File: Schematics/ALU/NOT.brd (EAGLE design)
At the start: 53.6 x 60 mm, 24 parts

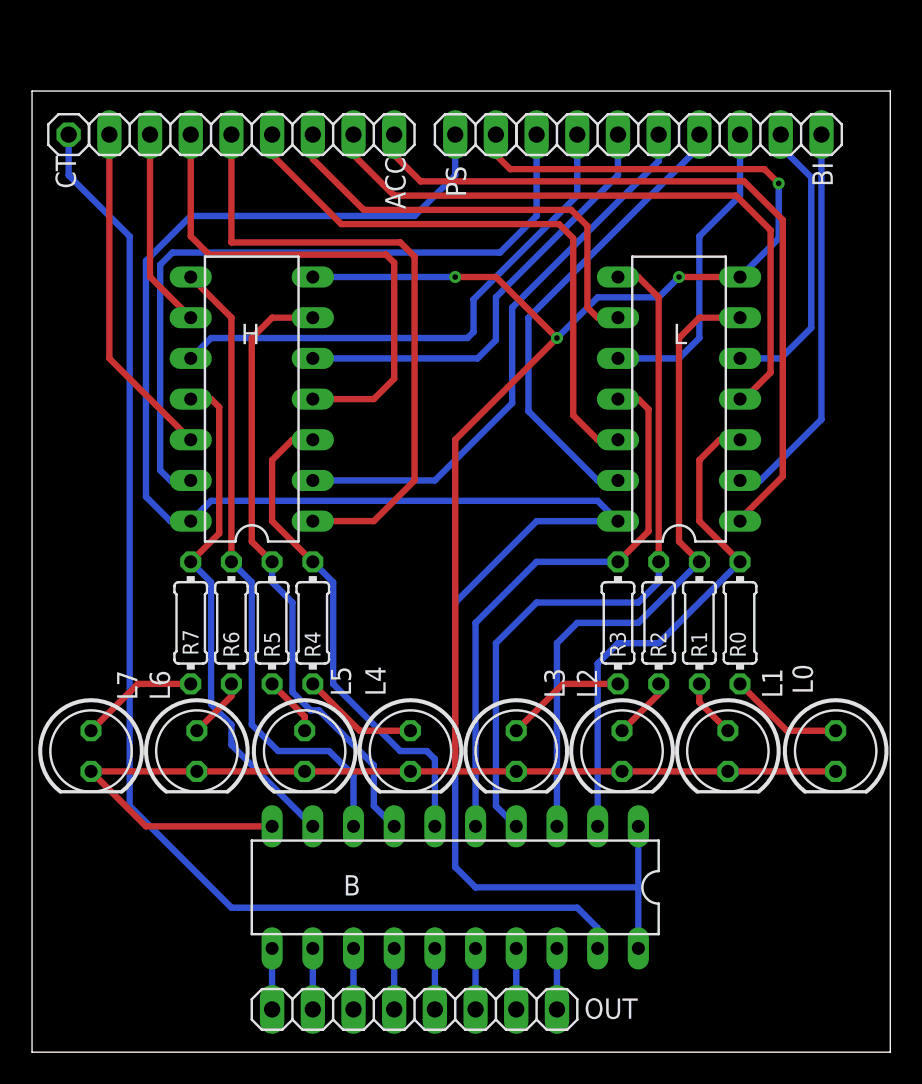
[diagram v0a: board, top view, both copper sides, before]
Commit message: Added NOT.
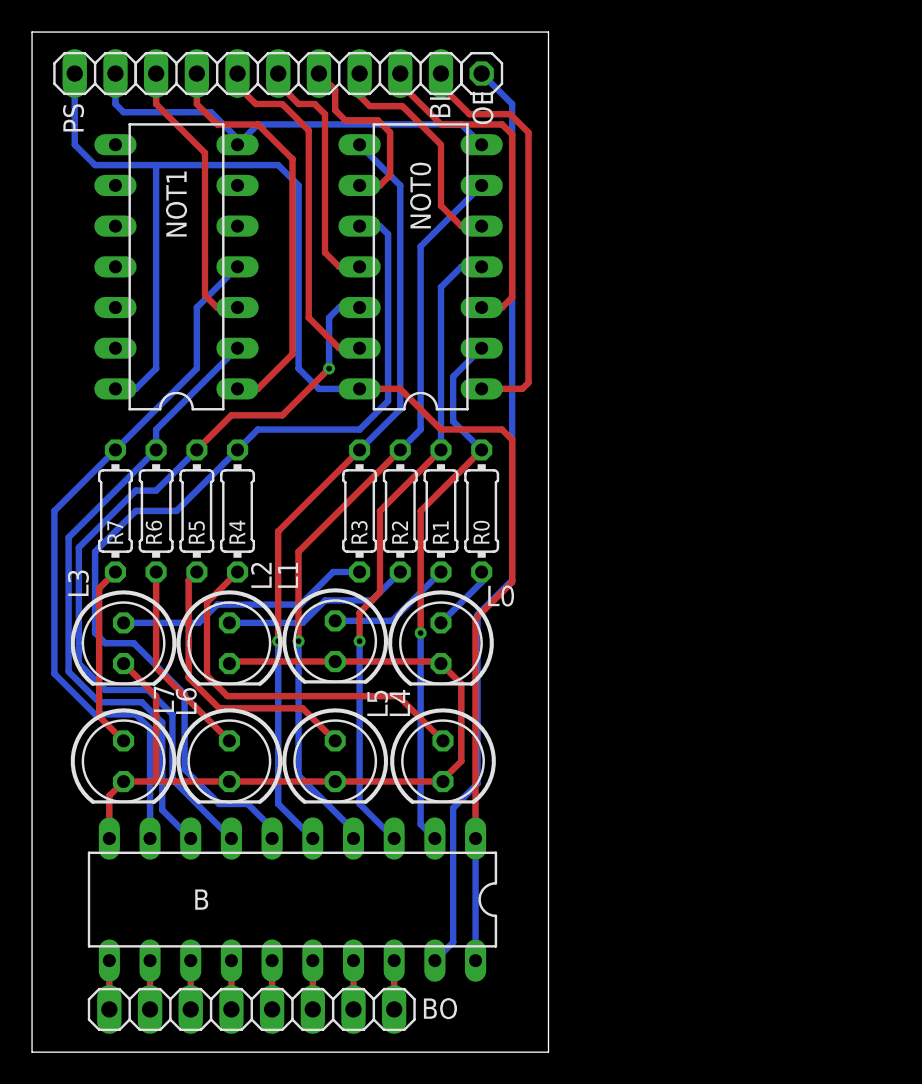
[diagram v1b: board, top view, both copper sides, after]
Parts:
- removed ACC, OUT: (no value), pinhead:1X08
- removed CT: (no value), pinhead:1X01
- removed H, L: 7408N, 74ttl-din:DIL14
- added BO: (no value), pinhead:1X08
- added NOT0, NOT1: 7404N, 74ttl-din:DIL14
- added OE: (no value), pinhead:1X01
- moved L0 25.5 mm to (25.5, 25.5)
- moved L1 25.5 mm to (18.9, 25.7)
- moved L3 25.4 mm to (5.71, 25.5)
- moved L2 25.4 mm to (12.3, 25.5)
- moved BI 24.1 mm to (16.6, 61.1)
- moved PS 24.1 mm to (3.94, 61.1)
- moved R2 17.6 mm to (23.0, 33.8)
- moved R3 17.6 mm to (20.4, 33.8)
- moved R0 17.6 mm to (28.1, 33.8)
- moved R1 17.6 mm to (25.5, 33.8)
- moved B 10.2 mm to (16.3, 9.53)
- moved R4 8.42 mm to (12.8, 33.8)
- moved R5 8.42 mm to (10.3, 33.8)
- moved R6 8.42 mm to (7.75, 33.8)
- moved R7 8.42 mm to (5.21, 33.8)
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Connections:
- removed net A0: ACC.8, L.1
- removed net A1: ACC.7, L.4
- removed net A2: ACC.6, L.9
- removed net A3: ACC.5, L.12
- removed net A4: ACC.4, H.1
- removed net A5: ACC.3, H.4
- removed net A6: ACC.2, H.9
- removed net A7: ACC.1, H.12
- net B0: now also NOT0.1; no longer L.2
- net B1: now also NOT0.3; no longer L.5
- net B2: now also NOT0.5; no longer L.10
- net B3: now also NOT0.9; no longer L.13
- net B4: now also NOT0.11; no longer H.2
- net B5: now also NOT0.13; no longer H.5
- net B6: now also NOT1.1; no longer H.10
- net B7: now also NOT1.3; no longer H.13
- net GND: now also NOT0.7, NOT1.7; no longer H.7, L.7
- net O0: now also BO.8; no longer OUT.8
- net O1: now also BO.7; no longer OUT.7
- net O2: now also BO.6; no longer OUT.6
- net O3: now also BO.5; no longer OUT.5
- net O4: now also BO.4; no longer OUT.4
- net O5: now also BO.3; no longer OUT.3
- net O6: now also BO.2; no longer OUT.2
- net O7: now also BO.1; no longer OUT.1
- net OE: now also OE.1; no longer CT.1
- net Q0: now also NOT0.2; no longer L.3
- net Q1: now also NOT0.4; no longer L.6
- net Q2: now also NOT0.6; no longer L.8
- net Q3: now also NOT0.8; no longer L.11
- net Q4: now also NOT0.10; no longer H.3
- net Q5: now also NOT0.12; no longer H.6
- net Q6: now also NOT1.2; no longer H.8
- net Q7: now also NOT1.4; no longer H.11
- net VCC: now also NOT0.14, NOT1.14; no longer H.14, L.14
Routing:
- net GND: track 145.2 -> 80.9 mm, vias 4 -> 0
- net A0: track 47.1 -> 0.00 mm
- net A1: track 40.7 -> 0.00 mm
- net A4: track 39.9 -> 0.00 mm
- net A3: track 36.7 -> 0.00 mm
- net A5: track 32.6 -> 0.00 mm
- net Q4: track 31.1 -> 59.1 mm
- net A2: track 27.7 -> 0.00 mm
- net B7: track 44.8 -> 17.5 mm
- net VCC: track 118.3 -> 95.3 mm
- net A7: track 21.2 -> 0.00 mm
- net B4: track 35.0 -> 15.5 mm
- net OE: track 77.1 -> 58.2 mm
- net B3: track 29.1 -> 11.5 mm
- net N$45: track 7.31 -> 23.7 mm
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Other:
- board size 53.6 x 60 mm -> 32.2 x 63.7 mm

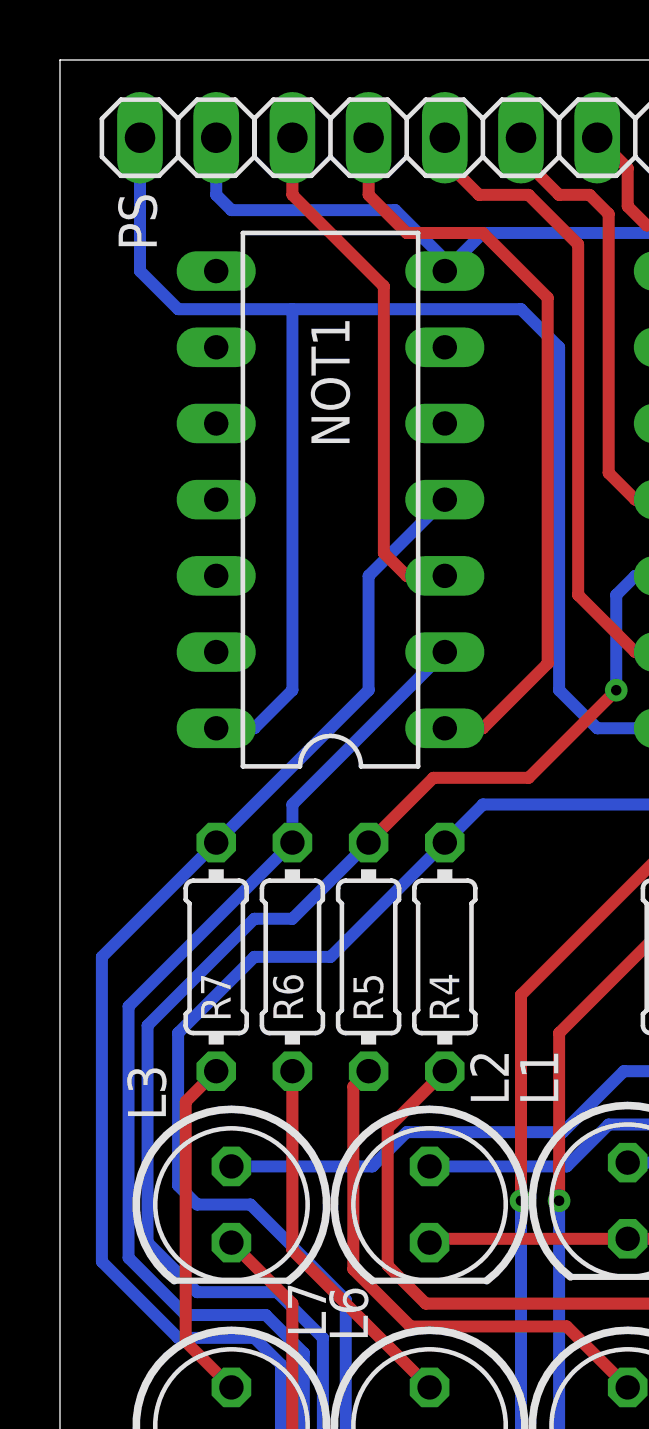
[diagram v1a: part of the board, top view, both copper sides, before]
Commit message: Fixed 2 problems, that I found after ordering boards
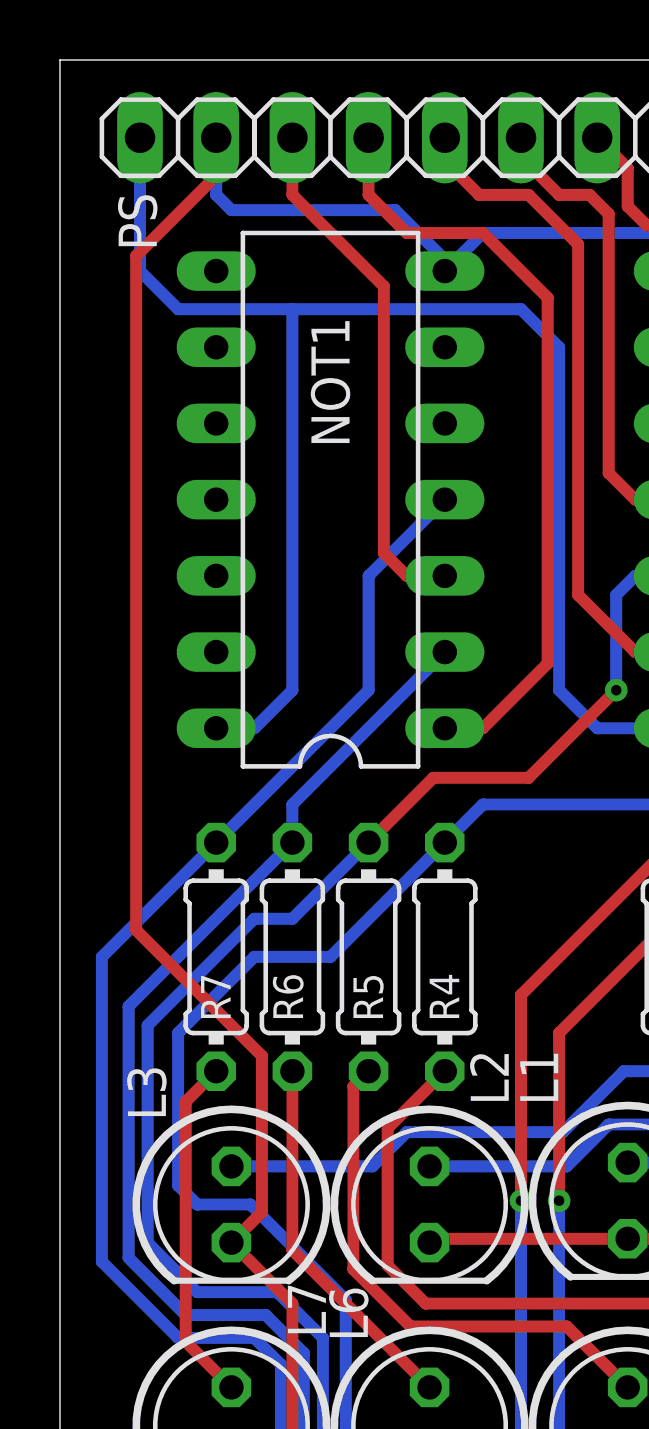
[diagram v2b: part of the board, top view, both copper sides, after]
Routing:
- net GND: track 80.9 -> 121.0 mm
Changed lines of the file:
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@@
 <wire x1="4.826" y1="13.335" x2="4.826" y2="16.002" width="0.4" layer="1"/>
 <wire x1="4.826" y1="16.002" x2="5.715" y2="16.891" width="0.4" layer="1"/>
-<wire x1="12.319" y1="24.257" x2="12.827" y2="56.642" width="0" layer="19" extent="1-1"/>
+<wire x1="5.715" y1="24.257" x2="6.731" y2="25.273" width="0.4" layer="1"/>
+<wire x1="5.207" y1="59.817" x2="5.207" y2="61.087" width="0.4" layer="1"/>
+<wire x1="6.731" y1="25.273" x2="6.731" y2="30.48" width="0.4" layer="1"/>
+<wire x1="6.731" y1="30.48" x2="2.54" y2="34.671" width="0.4" layer="1"/>
+<wire x1="2.54" y1="34.671" x2="2.54" y2="57.15" width="0.4" layer="1"/>
+<wire x1="2.54" y1="57.15" x2="5.207" y2="59.817" width="0.4" layer="1"/>
 </signal>
 <signal name="N$33">
